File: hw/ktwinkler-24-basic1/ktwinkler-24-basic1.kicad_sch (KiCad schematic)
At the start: 10 parts, among them SW1 RESET, SW2 BOOT, SW5 MODE

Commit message: ktwinkler-24: schematic "complete"
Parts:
- removed JP1: KJumper_3, Connector_PinHeader_2.54mm:PinHeader_1x03_P2.54mm_Vertical, symbol karl-parts:KJumper_3
- removed R11: 10k, Resistor_SMD:R_0402_1005Metric, symbol karl-atomic-basic:KR0402_10k
- removed SW1: RESET, Button_Switch_SMD:SW_SPST_TL3342, symbol Switch:SW_Push
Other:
- sheet esp32 ports: added none; removed P1IN, P1_Req_Out
- note added: "The only user button"
- note added: "kTwinkler-24"
- note removed: "Lower: held in reset Upper: button controlled Both open, reset floats..."
- note removed: "kTwinkler"

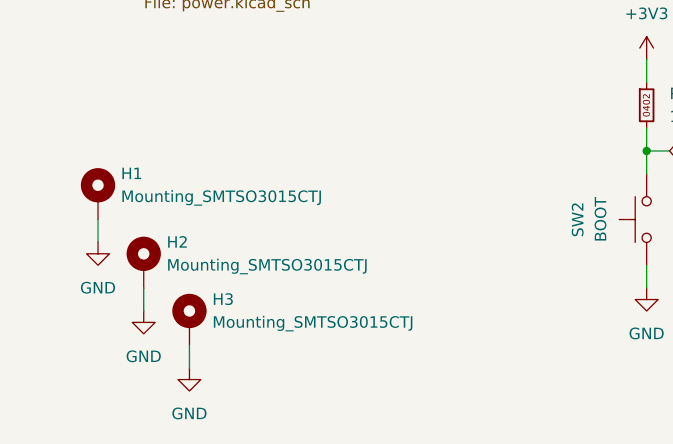
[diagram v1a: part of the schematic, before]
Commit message: 24-1: connect some planes that were independent
other little tidy ups
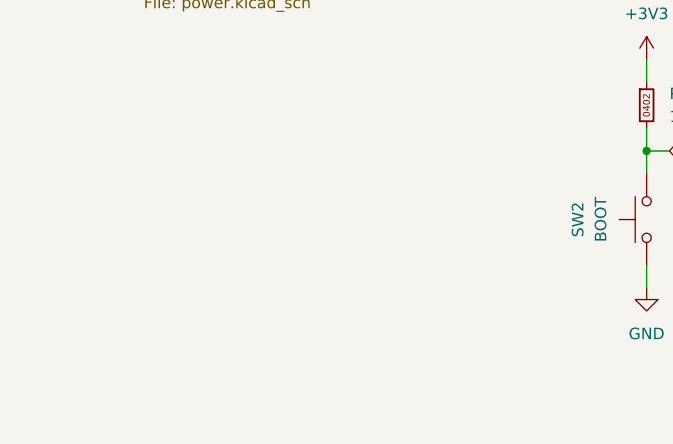
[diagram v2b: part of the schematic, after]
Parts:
- removed H1, H2, H3: Mounting_SMTSO3015CTJ, jlc-extras:Mounting_SMTSO_M3_ALT2, symbol karl-parts:Mounting_SMTSO3015CTJ

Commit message: k24-1: mounting, rounding labels
save point before retrying thigns
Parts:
- added H1, H2, H3: MountingHole, MountingHole:MountingHole_3.2mm_M3, symbol Mechanical:MountingHole
- added X1: (no value), jlc-extras:JLC_2D_BARCODE_8x8mm, symbol karl-atomic-basic:SYM_LABEL
